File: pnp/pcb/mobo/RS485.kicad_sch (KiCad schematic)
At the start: 4 parts, among them J17 Feeders, U14 MAX3078E

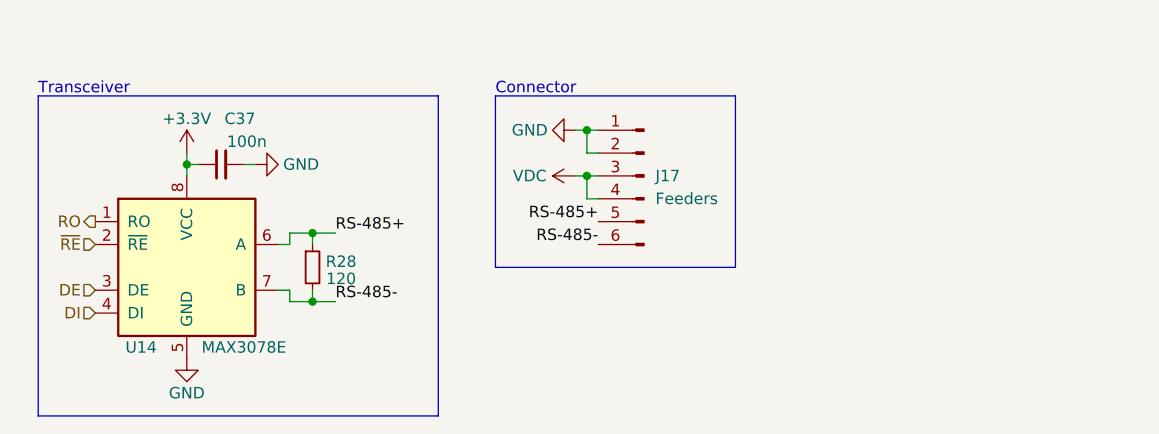
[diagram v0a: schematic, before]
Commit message: Mobo V4A Redesign
Some EMC improvements to schematics.
Reassigned MCU Pins for HW-PWM support.
Changes are still marked with text in the schematics.
Complete PCB Layout reworked
Status: Needs to be verified, and cleaned up a little, but DRC is running green.
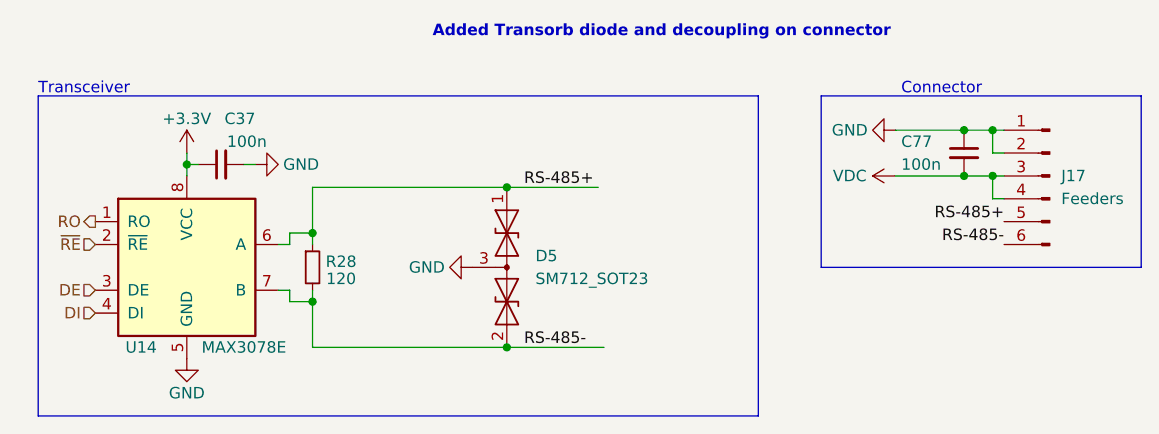
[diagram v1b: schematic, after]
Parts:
- added C77: 100n, Capacitor_SMD:C_0805_2012Metric, symbol Device:C_Small
- added D5: SM712_SOT23, Package_TO_SOT_SMD:SOT-23, symbol Diode:SM712_SOT23
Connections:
- net GND: now also C77.1, D5.3 (common)
- net RS-485+: now also D5.1 (A1)
- net RS-485-: now also D5.2 (A2)
- net VDC: now also C77.2
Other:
- note added: "Added Transorb diode and decoupling on connector"
- moved on the sheet: J17

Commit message: Redesign finished
Completed Board redesign and adding more EMC improvements.
Changed all the part numbers to have a Mouser orderable design (except the JST connectors)
All outputs generated
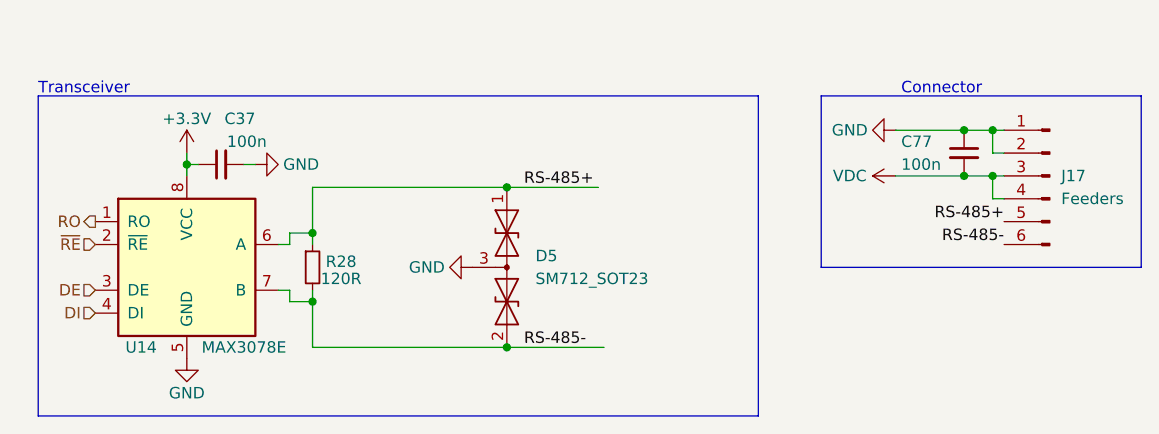
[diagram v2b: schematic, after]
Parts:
- C37, C77: Digikey 1276-1180-1-ND -> (none); JLCPCB C49678 -> (none); LCSC C360619 -> (none); Mouser 581-08055C104K -> 710-885012207098
- D5: Mouser (none) -> 947-SM712.TCT
- J17: JLCPCB C601936 -> (none); LCSC C601936 -> (none); Mouser (none) -> 538-87834-0619
- R28: value 120 -> 120R; Digikey 541-120CCT-ND -> (none); JLCPCB C17437 -> (none); LCSC C131390 -> (none); Mouser 71-CRCW0805120RFKEA -> 755-SDR10EZPF1200
- U14: JLCPCB C40031 -> (none); LCSC C40031 -> (none)
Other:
- note removed: "Added Transorb diode and decoupling on connector"
- company: Opulo -> Opulo.io
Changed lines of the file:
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@@
   (title_block
     (title "LumenPnP Motherboard")
-    (date "2022-09-09")
-    (rev "004A")
-    (company "Opulo")
+    (date "2022-10-06")
+    (rev "04A")
+    (company "Opulo.io")
     (comment 1 "Reengineered by Magpie")
   )
@@
   (text "Transceiver" (at 114.3 87.63 0)
     (effects (font (size 1.27 1.27)) (justify left bottom))
-  )
-  (text "Added Transorb diode and decoupling on connector" (at 158.115 81.28 0)
-    (effects (font (size 1.27 1.27) bold) (justify left bottom))
   )
   (text "Connector" (at 210.185 87.63 0)
@@
       (effects (font (size 1.27 1.27)) hide)
     )
+    (property "Mouser" "947-SM712.TCT" (id 4) (at 166.37 106.68 0)
+      (effects (font (size 1.27 1.27)) hide)
+    )
     (pin "1")
     (pin "2")
@@
       (effects (font (size 1.27 1.27)) hide)
     )
-    (property "Digikey" "1276-1180-1-ND" (id 4) (at 217.17 93.98 0)
-      (effects (font (size 1.27 1.27)) hide)
-    )
-    (property "JLCPCB" "C49678" (id 5) (at 217.17 93.98 0)
-      (effects (font (size 1.27 1.27)) hide)
-    )
-    (property "LCSC" "C360619" (id 6) (at 217.17 93.98 0)
-      (effects (font (size 1.27 1.27)) hide)
-    )
-    (property "Mouser" "581-08055C104K" (id 7) (at 217.17 93.98 0)
+    (property "Digikey" "" (id 4) (at 217.17 93.98 0)
+      (effects (font (size 1.27 1.27)) hide)
+    )
+    (property "JLCPCB" "" (id 5) (at 217.17 93.98 0)
+      (effects (font (size 1.27 1.27)) hide)
+    )
+    (property "LCSC" "" (id 6) (at 217.17 93.98 0)
+      (effects (font (size 1.27 1.27)) hide)
+    )
+    (property "Mouser" "710-885012207098" (id 7) (at 217.17 93.98 0)
       (effects (font (size 1.27 1.27)) hide)
     )
@@
       (effects (font (size 1.27 1.27)) hide)
     )
-    (property "LCSC" "C601936" (id 4) (at 226.695 96.52 0)
-      (effects (font (size 1.27 1.27)) hide)
-    )
-    (property "JLCPCB" "C601936" (id 5) (at 226.695 96.52 0)
+    (property "LCSC" "" (id 4) (at 226.695 96.52 0)
+      (effects (font (size 1.27 1.27)) hide)
+    )
+    (property "JLCPCB" "" (id 5) (at 226.695 96.52 0)
+      (effects (font (size 1.27 1.27)) hide)
+    )
+    (property "Mouser" "538-87834-0619" (id 6) (at 226.695 96.52 0)
       (effects (font (size 1.27 1.27)) hide)
     )
@@
     (in_bom yes) (on_board yes)
     (property "Reference" "R28" (id 0) (at 147.955 106.045 0))
-    (property "Value" "120" (id 1) (at 147.955 107.95 0))
+    (property "Value" "120R" (id 1) (at 147.955 107.95 0))
     (property "Footprint" "Resistor_SMD:R_0805_2012Metric" (id 2) (at 144.78 106.68 0)
       (effects (font (size 1.27 1.27)) hide)
     )
-    (property "Datasheet" "https://www.vishay.com/docs/20035/dcrcwe3.pdf" (id 3) (at 144.78 106.68 0)
-      (effects (font (size 1.27 1.27)) hide)
-    )
-    (property "Digikey" "541-120CCT-ND" (id 4) (at 144.78 106.68 0)
-      (effects (font (size 1.27 1.27)) hide)
-    )
-    (property "JLCPCB" " C17437" (id 5) (at 144.78 106.68 0)
-      (effects (font (size 1.27 1.27)) hide)
-    )
-    (property "LCSC" "C131390 " (id 6) (at 144.78 106.68 0)
-      (effects (font (size 1.27 1.27)) hide)
-    )
-    (property "Mouser" "71-CRCW0805120RFKEA" (id 7) (at 144.78 106.68 0)
+    (property "Datasheet" "" (id 3) (at 144.78 106.68 0)
+      (effects (font (size 1.27 1.27)) hide)
+    )
+    (property "Digikey" "" (id 4) (at 144.78 106.68 0)
+      (effects (font (size 1.27 1.27)) hide)
+    )
+    (property "JLCPCB" "" (id 5) (at 144.78 106.68 0)
+      (effects (font (size 1.27 1.27)) hide)
+    )
+    (property "LCSC" "" (id 6) (at 144.78 106.68 0)
+      (effects (font (size 1.27 1.27)) hide)
+    )
+    (property "Mouser" "755-SDR10EZPF1200" (id 7) (at 144.78 106.68 0)
       (effects (font (size 1.27 1.27)) hide)
     )
@@
       (effects (font (size 1.27 1.27)) hide)
     )
-    (property "Digikey" "1276-1180-1-ND" (id 4) (at 134.62 95.25 0)
-      (effects (font (size 1.27 1.27)) hide)
-    )
-    (property "JLCPCB" "C49678" (id 5) (at 134.62 95.25 0)
-      (effects (font (size 1.27 1.27)) hide)
-    )
-    (property "LCSC" "C360619" (id 6) (at 134.62 95.25 0)
-      (effects (font (size 1.27 1.27)) hide)
-    )
-    (property "Mouser" "581-08055C104K" (id 7) (at 134.62 95.25 0)
+    (property "Digikey" "" (id 4) (at 134.62 95.25 0)
+      (effects (font (size 1.27 1.27)) hide)
+    )
+    (property "JLCPCB" "" (id 5) (at 134.62 95.25 0)
+      (effects (font (size 1.27 1.27)) hide)
+    )
+    (property "LCSC" "" (id 6) (at 134.62 95.25 0)
+      (effects (font (size 1.27 1.27)) hide)
+    )
+    (property "Mouser" "710-885012207098" (id 7) (at 134.62 95.25 0)
       (effects (font (size 1.27 1.27)) hide)
     )
@@
       (effects (font (size 1.27 1.27)) hide)
     )
-    (property "LCSC" "C40031" (id 4) (at 130.81 106.68 0)
+    (property "LCSC" "" (id 4) (at 130.81 106.68 0)
       (effects (font (size 1.27 1.27)) hide)
     )
@@
       (effects (font (size 1.27 1.27)) hide)
     )
-    (property "JLCPCB" "C40031" (id 6) (at 130.81 106.68 0)
-      (effects (font (size 1.27 1.27)) hide)
-    )
+    (property "JLCPCB" "" (id 6) (at 130.81 106.68 0)
+      (effects (font (size 1.27 1.27)) hide)
+    )
